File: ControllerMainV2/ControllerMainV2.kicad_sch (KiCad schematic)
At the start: 13 parts, among them J1 Conn_01x07, J2 Conn_01x10, U1 MCP23009-E_SO, U2 MCP23009-E_SO

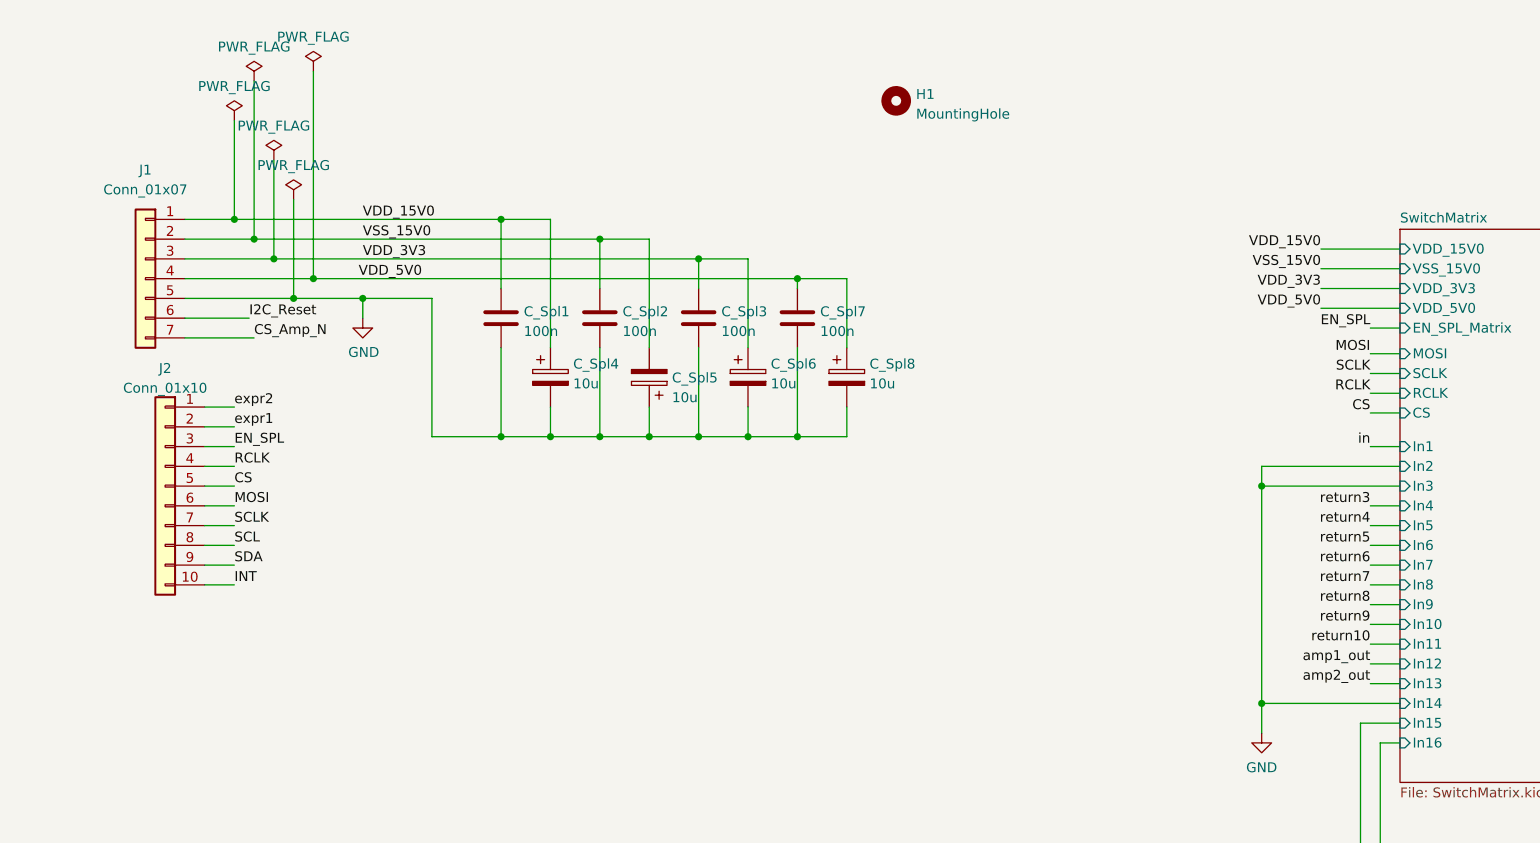
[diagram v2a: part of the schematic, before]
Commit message: Layout of PGAs
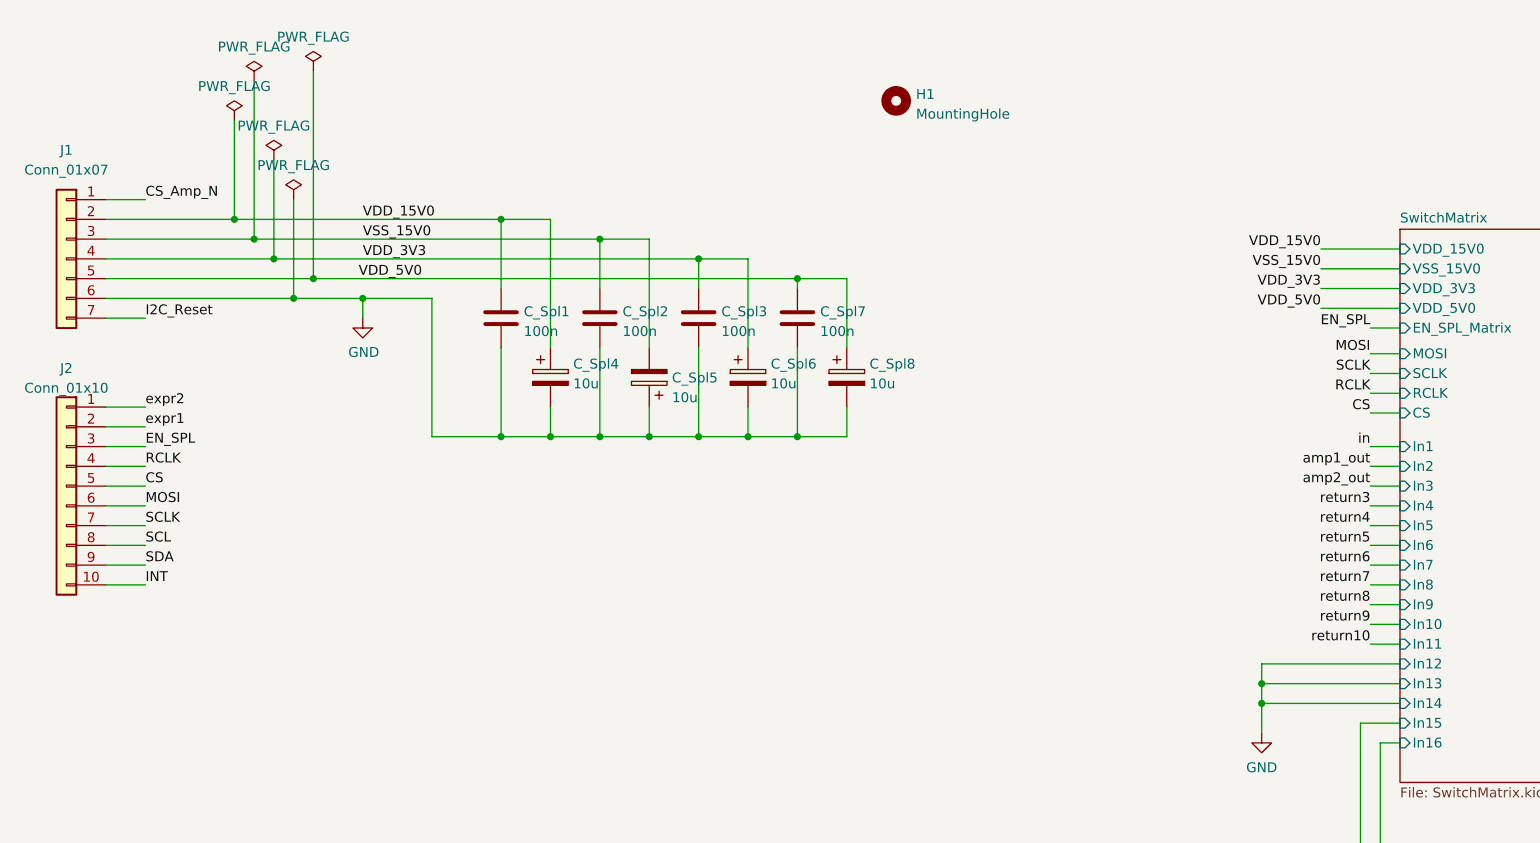
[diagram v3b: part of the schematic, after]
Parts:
- J1: footprint (none) -> Connector_JST:JST_PH_B7B-PH-K_1x07_P2.00mm_Vertical
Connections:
- net CS_Amp_N: now also J1.1 (Pin_1); no longer J1.7 (Pin_7)
- net GND: now also J1.6 (Pin_6); no longer J1.5 (Pin_5)
- net I2C_Reset: now also J1.7 (Pin_7); no longer J1.6 (Pin_6)
- net VDD_15V0: now also J1.2 (Pin_2); no longer J1.1 (Pin_1)
- net VDD_3V3: now also J1.4 (Pin_4); no longer J1.3 (Pin_3)
- net VDD_5V0: now also J1.5 (Pin_5); no longer J1.4 (Pin_4)
- net VSS_15V0: now also J1.3 (Pin_3); no longer J1.2 (Pin_2)
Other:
- moved on the sheet: J1, J2
